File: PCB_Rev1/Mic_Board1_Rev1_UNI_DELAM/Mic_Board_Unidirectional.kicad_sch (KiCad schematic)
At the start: 29 parts, among them J2 532610771, J3 S2B-ZR-SM4A-TF_LF__SN_, U1 OPA1671IDBVR

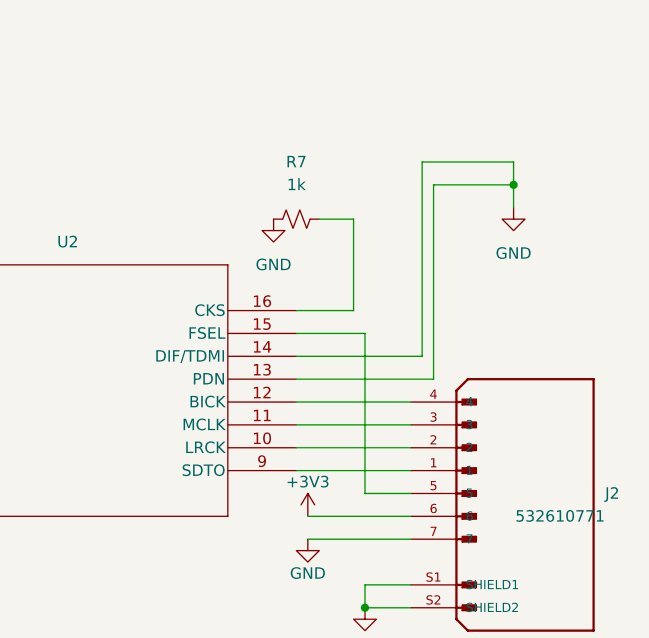
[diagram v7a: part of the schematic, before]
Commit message: connections for gpio and micboards
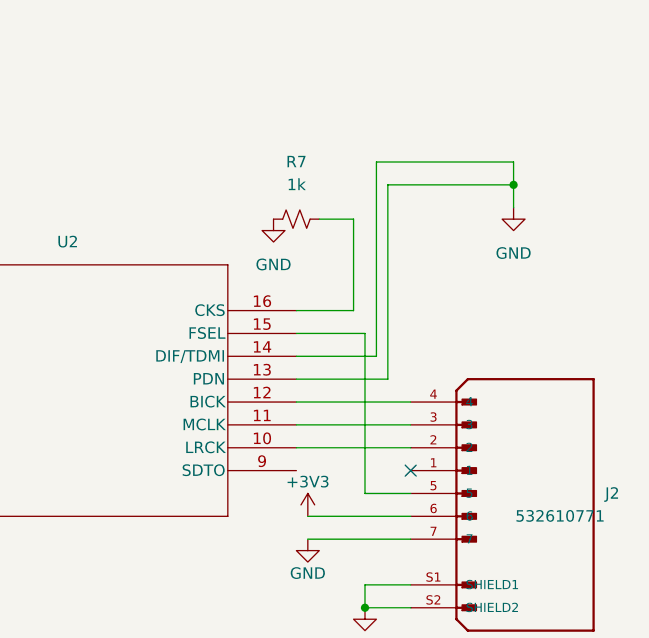
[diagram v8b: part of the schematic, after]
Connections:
- net at J2.1: no longer U2.9 (SDTO)
- no-connect marks 0 -> 1
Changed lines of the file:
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@@
 		(color 0 0 0 0)
 	)
+	(no_connect
+		(at 247.65 101.6)
+	)
 	(wire
 		(pts
@@
 	(wire
 		(pts
-			(xy 248.92 67.31) (xy 248.92 88.9)
-		)
-		(stroke
-			(width 0)
-			(type default)
-		)
-	)
-	(wire
-		(pts
-			(xy 248.92 88.9) (xy 234.95 88.9)
+			(xy 243.84 67.31) (xy 243.84 88.9)
+		)
+		(stroke
+			(width 0)
+			(type default)
+		)
+	)
+	(wire
+		(pts
+			(xy 243.84 88.9) (xy 234.95 88.9)
 		)
 		(stroke
@@
 	(wire
 		(pts
-			(xy 250.19 91.44) (xy 234.95 91.44)
+			(xy 245.11 91.44) (xy 234.95 91.44)
 		)
 		(stroke
@@
 	(wire
 		(pts
-			(xy 247.65 101.6) (xy 234.95 101.6)
-		)
-		(stroke
-			(width 0)
-			(type default)
-		)
-	)
-	(wire
-		(pts
 			(xy 91.44 121.92) (xy 97.79 121.92)
 		)
@@
 	(wire
 		(pts
-			(xy 250.19 69.85) (xy 259.08 69.85)
+			(xy 245.11 69.85) (xy 259.08 69.85)
 		)
 		(stroke
@@
 	(wire
 		(pts
-			(xy 248.92 67.31) (xy 259.08 67.31)
+			(xy 243.84 67.31) (xy 259.08 67.31)
 		)
 		(stroke
@@
 	(wire
 		(pts
-			(xy 250.19 69.85) (xy 250.19 91.44)
-		)
-		(stroke
+			(xy 245.11 69.85) (xy 245.11 91.44)
+		)
+		(stroke
